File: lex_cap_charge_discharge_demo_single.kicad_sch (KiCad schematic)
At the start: 8 parts, among them J1 +5V, J2 GND, SW1 charge, SW2 discharge

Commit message: put resistor next to +5v, tidy
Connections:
- net +5V: now also R1.1; no longer SW1.2 (B)
- net GND: now also C1.2; no longer R1.2
- new net: R1.2, SW1.2 (B)
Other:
- moved on the sheet: C1, D1, J1, J2, R1, R2, SW1, SW2

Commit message: Tweak R vals
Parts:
- R1: value 400K -> 10K
- R2: value 470 -> 330
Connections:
- net at C1.1, SW2.2 (B): now also SW1.2 (B); no longer SW1.1 (A)
- net at R1.2: now also SW1.1 (A); no longer SW1.2 (B)
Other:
- moved on the sheet: C1, D1, R1, R2, SW1, SW2

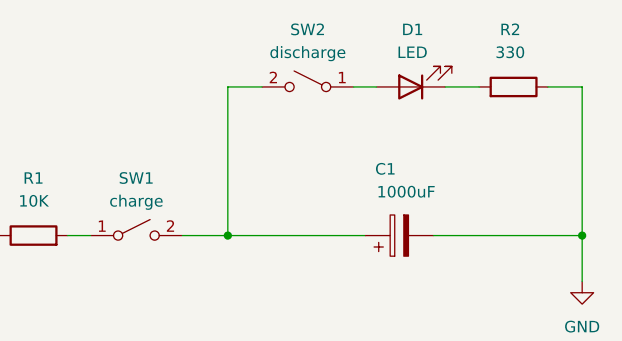
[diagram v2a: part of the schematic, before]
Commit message: Change various incl +V, GND solder pads; move components to  0.24mm standard pitch grid; add text front/back
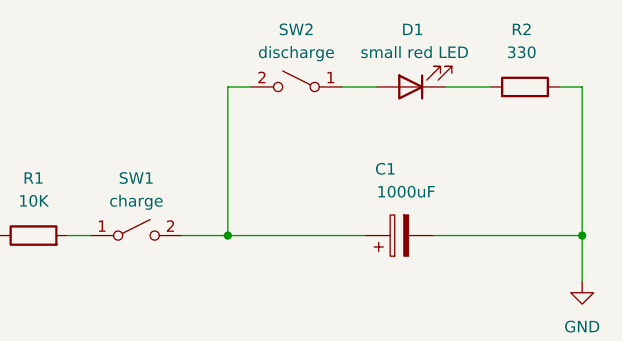
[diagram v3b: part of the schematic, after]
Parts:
- D1: value LED -> small red LED
- J1, J2: footprint Connector_Wire:SolderWire-0.1sqmm_1x01_D0.4mm_OD1mm -> TestPoint:TestPoint_THTPad_2.0x2.0mm_Drill1.0mm
- SW1, SW2: footprint Button_Switch_THT:SW_Tactile_Straight_KSL0Axx1LFTR -> Button_Switch_THT:SW_PUSH_6mm_H4.3mm
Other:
- moved on the sheet: R2, SW2
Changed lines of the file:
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@@
 	(wire
 		(pts
-			(xy 53.34 29.21) (xy 57.15 29.21)
+			(xy 53.34 29.21) (xy 55.88 29.21)
 		)
 		(stroke
@@
 	(wire
 		(pts
-			(xy 88.9 29.21) (xy 92.71 29.21)
+			(xy 90.17 29.21) (xy 92.71 29.21)
 		)
 		(stroke
@@
 	(wire
 		(pts
-			(xy 67.31 29.21) (xy 69.85 29.21)
+			(xy 66.04 29.21) (xy 69.85 29.21)
 		)
 		(stroke
@@
 	(wire
 		(pts
-			(xy 77.47 29.21) (xy 81.28 29.21)
+			(xy 77.47 29.21) (xy 82.55 29.21)
 		)
 		(stroke
@@
 	(symbol
 		(lib_id "Device:R")
-		(at 85.09 29.21 270)
+		(at 86.36 29.21 270)
 		(mirror x)
 		(unit 1)
@@
 		(dnp no)
 		(property "Reference" "R2"
-			(at 83.566 22.86 90)
+			(at 84.836 22.86 90)
 			(effects
 				(font
@@
 		)
 		(property "Value" "330"
-			(at 83.058 25.4 90)
+			(at 84.328 25.4 90)
 			(effects
 				(font
@@
 		)
 		(property "Footprint" "Resistor_THT:R_Axial_DIN0204_L3.6mm_D1.6mm_P7.62mm_Horizontal"
-			(at 85.09 30.988 90)
+			(at 86.36 30.988 90)
 			(effects
 				(font
@@
 		)
 		(property "Datasheet" "~"
-			(at 85.09 29.21 0)
+			(at 86.36 29.21 0)
 			(effects
 				(font
@@
 		)
 		(property "Description" "Resistor"
-			(at 85.09 29.21 0)
+			(at 86.36 29.21 0)
 			(effects
 				(font
@@
 			)
 		)
-		(property "Footprint" "Connector_Wire:SolderWire-0.1sqmm_1x01_D0.4mm_OD1mm"
+		(property "Footprint" "TestPoint:TestPoint_THTPad_2.0x2.0mm_Drill1.0mm"
 			(at 25.4 71.12 0)
 			(effects
@@
 			)
 		)
-		(property "Value" "LED"
-			(at 72.136 25.4 0)
+		(property "Value" "small red LED"
+			(at 68.072 25.4 0)
 			(effects
 				(font
@@
 	(symbol
 		(lib_id "Switch:SW_SPST")
-		(at 62.23 29.21 0)
+		(at 60.96 29.21 0)
 		(mirror y)
 		(unit 1)
@@
 		(dnp no)
 		(property "Reference" "SW2"
-			(at 62.23 22.86 0)
+			(at 60.96 22.86 0)
 			(effects
 				(font
@@
 		)
 		(property "Value" "discharge"
-			(at 62.23 25.4 0)
-			(effects
-				(font
-					(size 1.27 1.27)
-				)
-			)
-		)
-		(property "Footprint" "Button_Switch_THT:SW_Tactile_Straight_KSL0Axx1LFTR"
-			(at 62.23 29.21 0)
+			(at 60.96 25.4 0)
+			(effects
+				(font
+					(size 1.27 1.27)
+				)
+			)
+		)
+		(property "Footprint" "Button_Switch_THT:SW_PUSH_6mm_H4.3mm"
+			(at 60.96 29.21 0)
 			(effects
 				(font
@@
 		)
 		(property "Datasheet" "~"
-			(at 62.23 29.21 0)
+			(at 60.96 29.21 0)
 			(effects
 				(font
@@
 		)
 		(property "Description" "Single Pole Single Throw (SPST) switch"
-			(at 62.23 29.21 0)
+			(at 60.96 29.21 0)
 			(effects
 				(font
@@
 			)
 		)
-		(property "Footprint" "Connector_Wire:SolderWire-0.1sqmm_1x01_D0.4mm_OD1mm"
+		(property "Footprint" "TestPoint:TestPoint_THTPad_2.0x2.0mm_Drill1.0mm"
 			(at 25.4 81.28 0)
 			(effects
@@
 			)
 		)
-		(property "Footprint" "Button_Switch_THT:SW_Tactile_Straight_KSL0Axx1LFTR"
+		(property "Footprint" "Button_Switch_THT:SW_PUSH_6mm_H4.3mm"
 			(at 43.18 45.72 0)
 			(effects

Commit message: Tweak, add title
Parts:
- D1: value small red LED -> 3mm red LED
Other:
- note added: "2025-05-20"
- note added: "cap-fun"
- note added: "momentary"
- moved on the sheet: C1, D1, R1, R2, SW1, SW2
